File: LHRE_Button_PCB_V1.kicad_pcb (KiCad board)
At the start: 2 copper layers, 146.5 x 78.7 mm, 78 parts, among them IC1 LM5155DSSR, IC2 LM5155DSSR, J1 Conn_01x12_Female, J2 Conn_01x12_Female, J3 Conn_01x02_Female, J4 Conn_01x02_Female, Q1 CSD18537NQ5A, Q2 CSD18537NQ5A, SW1 Dashboard_Button, SW2 Dashboard_Button, SW3 Dashboard_Button, SW4 Dashboard_Button, SW5 Dashboard_Button, SW6 Dashboard_Button

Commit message: REV2
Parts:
- removed C13, C14, C16: 10u, Capacitor_SMD:C_0603_1608Metric
- removed C15, C22: 100p, Capacitor_SMD:C_0603_1608Metric
- removed C17: 270p, Capacitor_SMD:C_0603_1608Metric
- removed C18: 100n, Capacitor_SMD:C_0603_1608Metric
- removed C19: 220n, Capacitor_SMD:C_0603_1608Metric
- removed C20: 6.8n, Capacitor_SMD:C_0603_1608Metric
- removed C21: 1u, Capacitor_SMD:C_0603_1608Metric
- removed C23: 9.4u, Capacitor_SMD:C_0603_1608Metric
- removed C24: 66u, Capacitor_SMD:C_0603_1608Metric
- removed the D1 at (88.5, 62.5)
- removed D2: LED, Connector_Wire:SolderWire-0.75sqmm_1x02_P4.8mm_D1.25mm_OD2.3mm
- removed D4: STPS20M100SG-TR, Global Libraries_2:STPS20M100SG-TR
- removed IC2: LM5155DSSR, Global Libraries_2:SON50P200X300X80-13N-D
- removed L2: 7448700015, Inductor Thing:WE-DD_12XX_CROSSED12
- removed Q2: CSD18537NQ5A, Global Libraries_2:CSD19531Q5AT
- removed the R21 at (182.1, 87.6)
- removed the R22 at (186.2, 89.6)
- removed the R23 at (182.1, 85.8)
- removed the R24 at (182.1, 84.0)
- removed the R25 at (189.3, 45.5)
- removed the R26 at (185.7, 45.5)
- removed the R7 at (204.6, 80.7)
- removed the SW4 at (199.9, 44.8)
- added J5: Conn_01x08, Connector_Molex:Molex_Micro-Fit_3.0_43650-0800_1x08_P3.00mm_Horizontal, F.Cu at (172.0, 80.0)
- added J6: Conn_01x12, Connector_Molex:Molex_Micro-Fit_3.0_43045-1212_2x06_P3.00mm_Vertical, F.Cu at (222.0, 51.0)
- added J7: Conn_01x02, Connector_Molex:Molex_Micro-Fit_3.0_43650-0215_1x02_P3.00mm_Vertical, F.Cu at (109.0, 76.0)
- added R1: 10k, Resistor_SMD:R_0603_1608Metric, F.Cu at (142.5, 40.0)
- added R10: 470, Resistor_SMD:R_0603_1608Metric, F.Cu at (125.5, 76.7)
- added R11: 470, Resistor_SMD:R_0603_1608Metric, F.Cu at (127.9, 95.9)
- added R12: 10k, Resistor_SMD:R_0603_1608Metric, F.Cu at (178.8, 56.5)
- added R13: 10k, Resistor_SMD:R_0603_1608Metric, F.Cu at (176.3, 56.5)
- added R14: 10k, Resistor_SMD:R_0603_1608Metric, F.Cu at (180.8, 83.5)
- added R15: 10k, Resistor_SMD:R_0603_1608Metric, F.Cu at (178.3, 83.5)
- added R16: 10k, Resistor_SMD:R_0603_1608Metric, F.Cu at (178.9, 102.6)
- added R17: 10k, Resistor_SMD:R_0603_1608Metric, F.Cu at (176.3, 102.6)
- added R9: 470, Resistor_SMD:R_0603_1608Metric, F.Cu at (127.8, 50.2)
- added SW1: SW_DIP_x06, Through_DIP_6:18253604, F.Cu at (145.0, 44.4)
- added SW10: Dashboard_Button, Dashboard_LED:Dashboard_Btn, F.Cu at (199.9, 44.8)
- added SW11: Dashboard_Button, Dashboard_LED:Dashboard_Btn, F.Cu at (199.9, 65.1)
- added SW12: Dashboard_Button, Dashboard_LED:Dashboard_Btn, F.Cu at (199.9, 85.4)
- added SW7: SW_DIP_x06, Through_DIP_6:18253604, F.Cu at (176.3, 52.0)
- added SW8: SW_DIP_x06, Through_DIP_6:18253604, F.Cu at (178.3, 79.1)
- added SW9: SW_DIP_x06, Through_DIP_6:18253604, F.Cu at (176.3, 98.1)
- C1, C10, C11, C12, C2, C3, C4, C5, C6, C7, C8, C9, IC1, L1, Q1: moved to B.Cu
- D1: renamed from D3; moved to B.Cu
- J1, J2: value Conn_01x12_Female -> Conn_01x02; footprint Connector_Molex:Molex_Micro-Fit_3.0_43650-1210_1x12-1MP_P3.00mm_Horizontal -> Connector_Molex:Molex_Micro-Fit_3.0_43650-0215_1x02_P3.00mm_Vertical
- J3: value Conn_01x02_Female -> Conn_01x02; footprint Connector_Molex:Molex_Micro-Fit_3.0_43650-0210_1x02-1MP_P3.00mm_Horizontal -> Connector_Molex:Molex_Micro-Fit_3.0_43650-0215_1x02_P3.00mm_Vertical
- J4: value Conn_01x02_Female -> Conn_01x08; footprint Connector_Wire:SolderWire-0.75sqmm_1x02_P4.8mm_D1.25mm_OD2.3mm -> Connector_Molex:Molex_Micro-Fit_3.0_43650-0800_1x08_P3.00mm_Horizontal
- R18: value 6k8 -> 470
- R19: value 34k8 -> 470
- R2, R3, R4, R5, R6: value 1K -> 10k
- R20: value 17k8 -> 470
- R21: renamed from R9; moved to B.Cu
- R22: renamed from R10; moved to B.Cu
- R23: renamed from R11; moved to B.Cu
- R24: renamed from R12; moved to B.Cu
- R25: renamed from R13; moved to B.Cu
- R26: renamed from R14; moved to B.Cu
- R27: renamed from R15; moved to B.Cu
- R28: renamed from R16; moved to B.Cu
- R29: renamed from R17; moved to B.Cu
- SW2, SW3: value Dashboard_Button -> SW_DIP_x06; footprint Dashboard_LED:Dashboard_Btn -> Through_DIP_6:18253604
- moved SW5 78.0 mm to (122.0, 65.1)
- moved SW6 78.0 mm to (122.0, 85.4)
- moved R5 76.9 mm to (142.5, 86.0), turned to -90 degrees
- moved R6 64.9 mm to (145.0, 86.0), turned to -90 degrees
- moved J2 46.0 mm to (208.2, 53.2), turned to -90 degrees
- moved R18 43.2 mm to (193.2, 50.8), turned to -90 degrees
- moved J1 42.0 mm to (109.0, 56.0), turned to 90 degrees
- moved J3 41.9 mm to (208.1, 73.6), turned to -90 degrees
- moved SW3 38.8 mm to (145.0, 90.5), turned to -90 degrees
- moved SW2 36.8 mm to (142.8, 71.5), turned to -90 degrees
- moved R4 34.5 mm to (142.9, 67.1), turned to -90 degrees
- moved R2 33.9 mm to (145.0, 40.0), turned to -90 degrees
- moved C2 32.8 mm to (149.6, 85.8)
- moved J4 32.2 mm to (149.2, 59.0), turned to -90 degrees
- moved C4 29.9 mm to (147.8, 85.8)
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- renumbered R1 to R7, SW1 to SW4
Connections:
- J1 pad 1: AMS -> Net-(J1-Pad1)
- J1 pad 2: 12V_L -> GND1
- J2 pad 1: GND -> Net-(J2-Pad1)
- J2 pad 2: Vin_R -> GND
- J3 pad 2: SHTDWN_OUT -> INRTA_IN_R
- J4 pad 1: SHTDWN_IN -> SW1_OUT
- J4 pad 2: SHTDWN_OUT -> AMS
- R18 pad 1: /SEPIC_CAD_R/UVLO -> G41
- R18 pad 2: GND -> Net-(R18-Pad2)
- R19 pad 1: Vin_R -> G51
- R19 pad 2: /SEPIC_CAD_R/UVLO -> Net-(R19-Pad2)
- R2 pad 2: SW1_OUT -> Net-(R2-Pad2)
- R20 pad 1: GND -> G61
- R20 pad 2: /SEPIC_CAD_R/RT -> Net-(R20-Pad2)
- R3 pad 1: GND1 -> 12V_L
- R3 pad 2: SW2_OUT -> Net-(R3-Pad2)
- R4 pad 2: SW3_OUT -> Net-(R4-Pad2)
- R5 pad 1: GND -> 12V_L
- R5 pad 2: SW4_OUT -> Net-(R5-Pad2)
- R6 pad 1: GND -> GND1
- R6 pad 2: SW5_OUT -> Net-(R6-Pad2)
- R7 pad 2: Net-(D1-Pad2) -> Net-(J1-Pad1)
- R8 pad 2: Net-(D2-Pad2) -> Net-(J2-Pad1)
- SW2 pad 1: 12V_L -> Net-(R4-Pad2)
- SW2 pad 2: SW2_OUT -> Net-(R3-Pad2)
- SW2 pad 3: unconnected-(SW2-Pad3) -> SW2_OUT
- SW2 pad 4: MCU_SIG2 -> SW2_OUT
- SW2 pad 5: GND1 -> 12V_L
- SW3 pad 1: 12V_L -> Net-(R6-Pad2)
- SW3 pad 2: SW3_OUT -> Net-(R5-Pad2)
- SW3 pad 3: unconnected-(SW3-Pad3) -> SW3_OUT
- SW3 pad 4: MCU_SIG3 -> SW3_OUT
- SW3 pad 5: GND1 -> 12V_L
- SW4 pad 1: 12V_L -> SW1_IN
- SW4 pad 4: MCU_SIG1 -> P11
- SW4 pad 5: GND1 -> Net-(R9-Pad2)
- SW5 pad 1: 12V_R -> SW2_IN
- SW5 pad 2: SW5_OUT -> SW2_OUT
- SW5 pad 4: MCU_SIG5 -> P21
- SW5 pad 5: GND -> Net-(R10-Pad2)
- SW6 pad 1: 12V_R -> SW3_IN
- SW6 pad 2: SW6_OUT -> SW3_OUT
- SW6 pad 4: MCU_SIG6 -> P31
- SW6 pad 5: GND -> Net-(R11-Pad2)
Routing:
- net 12V_L: track 181.4 -> 92.4 mm, vias 0 -> 1
- net /SEPIC_CAD_R/FB: track 69.1 -> 0.00 mm
- net MCU_SIG3: track 60.9 -> 0.00 mm, vias 2 -> 0
- net SW3_OUT_R: track 0.00 -> 59.5 mm, vias 0 -> 2
- net GND: track 55.8 -> 0.00 mm, vias 18 -> 9
- net SW1_OUT_R: track 0.00 -> 55.3 mm
- net SW2_OUT_R: track 0.00 -> 54.8 mm
- net SHTDWN_OUT_R: track 0.00 -> 51.8 mm
- net AMS_R: track 0.00 -> 50.3 mm
- net MCU_SIG1: track 46.6 -> 0.00 mm
- net MCU_SIG2: track 46.6 -> 0.00 mm
- net INRTA_IN: track 0.00 -> 44.3 mm, vias 0 -> 2
- net 12V_R: track 139.7 -> 96.0 mm
- net SW2_IN: track 0.00 -> 43.2 mm
- net Net-(C11-Pad1): track 16.6 -> 58.7 mm
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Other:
- board size 146.5 x 78.7 mm -> 131.7 x 78.7 mm

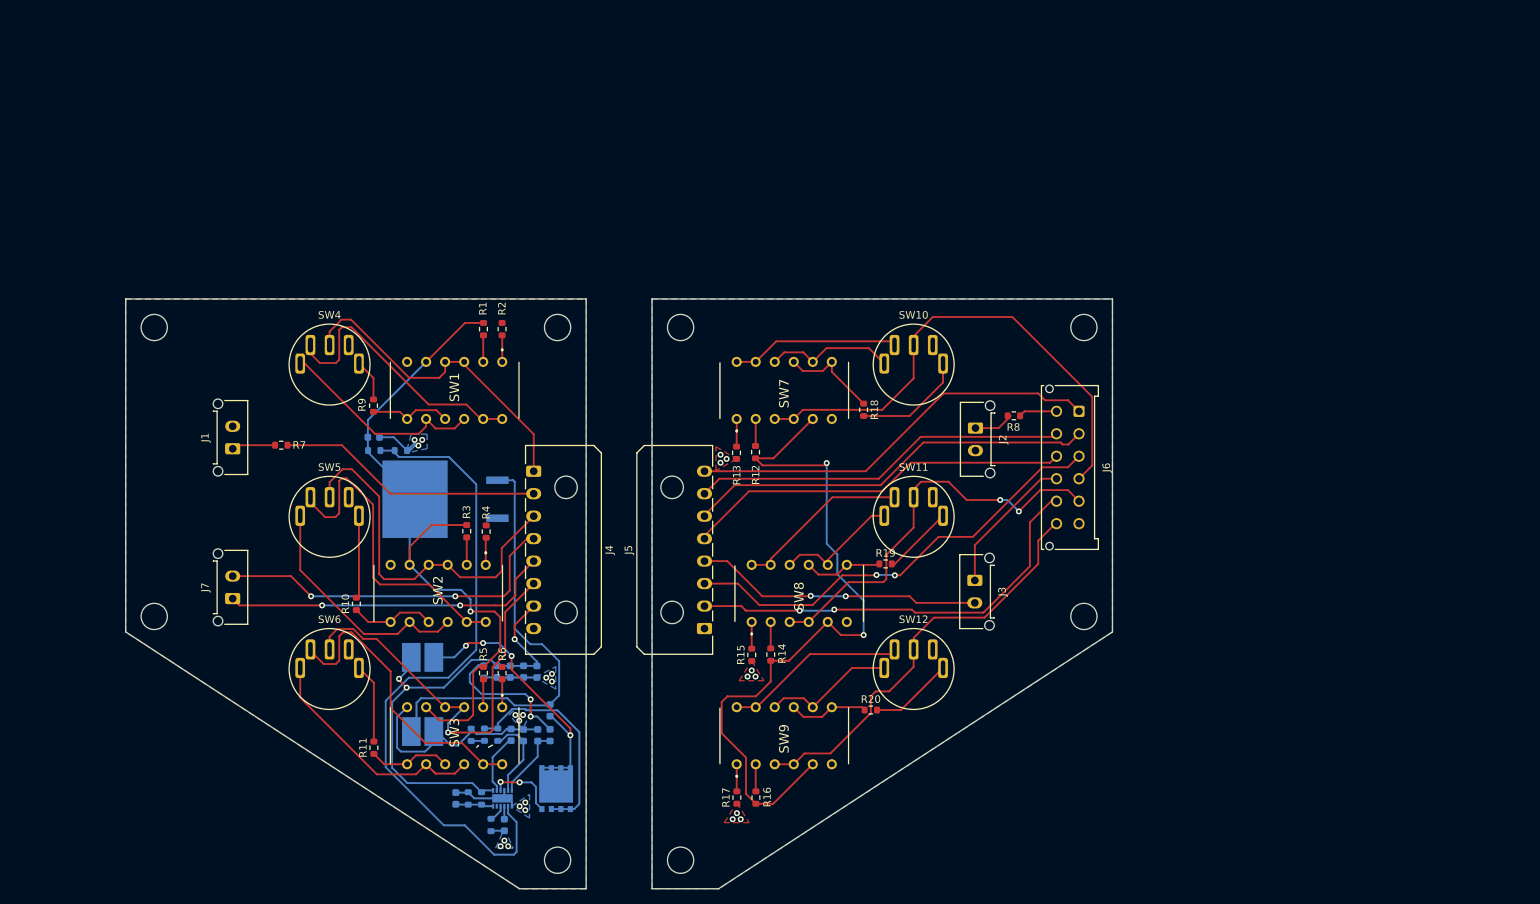
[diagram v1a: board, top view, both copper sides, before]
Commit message: flipped connectors
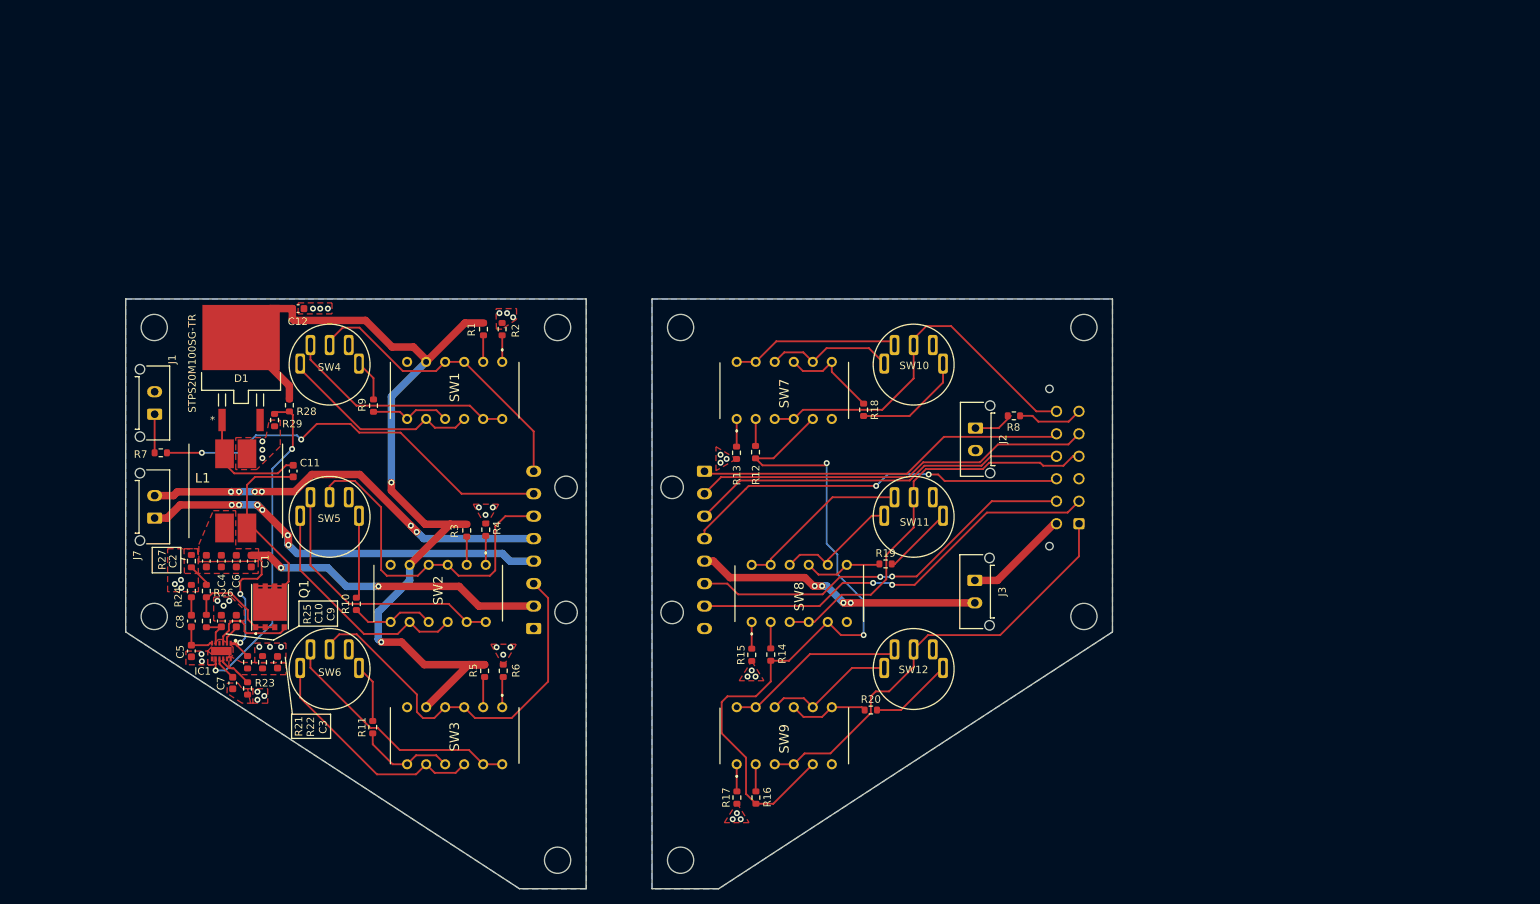
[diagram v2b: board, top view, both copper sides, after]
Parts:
- C1, C10, C11, C12, C2, C3, C4, C5, C6, C7, C8, C9, D1, IC1, L1, Q1, R21, R22, R23, R24, R25, R26, R27, R28, R29: moved to F.Cu
- J4, J5, J6: moved to B.Cu
- moved C8 50.3 mm to (103.5, 79.0)
- moved C5 47.6 mm to (103.5, 83.0), turned to -90 degrees
- moved C11 46.9 mm to (117.1, 59.0)
- moved C2 46.5 mm to (105.5, 71.0)
- moved Q1 45.3 mm to (114.0, 77.4)
- moved R27 44.0 mm to (103.5, 71.0)
- moved C10 43.1 mm to (107.5, 79.0)
- moved C4 43.0 mm to (107.5, 71.0)
- moved IC1 42.4 mm to (107.5, 83.0)
- moved R26 41.8 mm to (105.5, 75.0), turned to 90 degrees
- moved R25 41.8 mm to (105.5, 79.0)
- moved C7 40.9 mm to (109.0, 87.3)
- moved R24 40.5 mm to (103.5, 75.0), turned to 90 degrees
- moved C9 39.7 mm to (109.5, 79.0)
- moved C6 39.4 mm to (109.5, 71.0)
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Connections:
- J4 pad 1: SW1_OUT -> GND1
- J4 pad 2: AMS -> Vin_L
- J4 pad 3: SW2_OUT -> SW3_OUT
- J4 pad 4: SHTDWN_OUT -> INRTA_IN
- J4 pad 5: INRTA_IN -> SHTDWN_OUT
- J4 pad 6: SW3_OUT -> SW2_OUT
- J4 pad 7: Vin_L -> AMS
- J4 pad 8: GND1 -> SW1_OUT
- J5 pad 1: GND -> SW1_OUT_R
- J5 pad 2: Vin_R -> AMS_R
- J5 pad 3: SW3_OUT_R -> SW2_OUT_R
- J5 pad 4: INRTA_IN_R -> SHTDWN_OUT_R
- J5 pad 5: SHTDWN_OUT_R -> INRTA_IN_R
- J5 pad 6: SW2_OUT_R -> SW3_OUT_R
- J5 pad 7: AMS_R -> Vin_R
- J5 pad 8: SW1_OUT_R -> GND
- J6 pad 1: SW1_OUT_R -> SW6_OUT
- J6 pad 10: SHTDWN_IN -> SW2_OUT_R
- J6 pad 11: Vin_R -> SW1_OUT_R
- J6 pad 12: SW6_OUT -> SW4_OUT
- J6 pad 2: SW2_OUT_R -> Vin_R
- J6 pad 3: SW3_OUT_R -> GND
- J6 pad 4: SW4_OUT -> SW5_OUT
- J6 pad 5: SW5_OUT -> AMS_R
- J6 pad 6: GND -> IMD
- J6 pad 7: IMD -> SHTDWN_IN
- J6 pad 8: AMS_R -> SW3_OUT_R
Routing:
- net GND1: track 56.7 -> 0.07 mm, vias 15 -> 29
- net /SEPIC_CAD/FB: track 89.7 -> 43.5 mm, vias 0 -> 2
- net Net-(C11-Pad1): track 58.7 -> 16.1 mm
- net 12V_L: track 92.4 -> 127.0 mm, vias 1 -> 2
- net AMS: track 35.6 -> 54.9 mm, vias 0 -> 2
- net SW4_OUT: track 67.4 -> 50.6 mm
- net Net-(C8-Pad2): track 18.1 -> 2.40 mm, vias 2 -> 0
- net Net-(Q1-Pad1): track 29.0 -> 14.3 mm
- net INRTA_IN: track 44.3 -> 58.4 mm, vias 2 -> 6
- net SHTDWN_OUT: track 47.2 -> 58.5 mm, vias 2 -> 6
- net Net-(C11-Pad2): track 37.8 -> 27.0 mm, vias 4 -> 0
- net SW2_IN: track 43.2 -> 35.6 mm
- net Net-(C10-Pad2): track 11.6 -> 4.51 mm
- net SW3_IN: track 40.3 -> 33.4 mm
- net SW3_OUT_R: track 59.5 -> 52.7 mm
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- added copper zone on F.Cu, net /SEPIC_CAD/UVLO
- added copper zone on F.Cu, net Vin_L

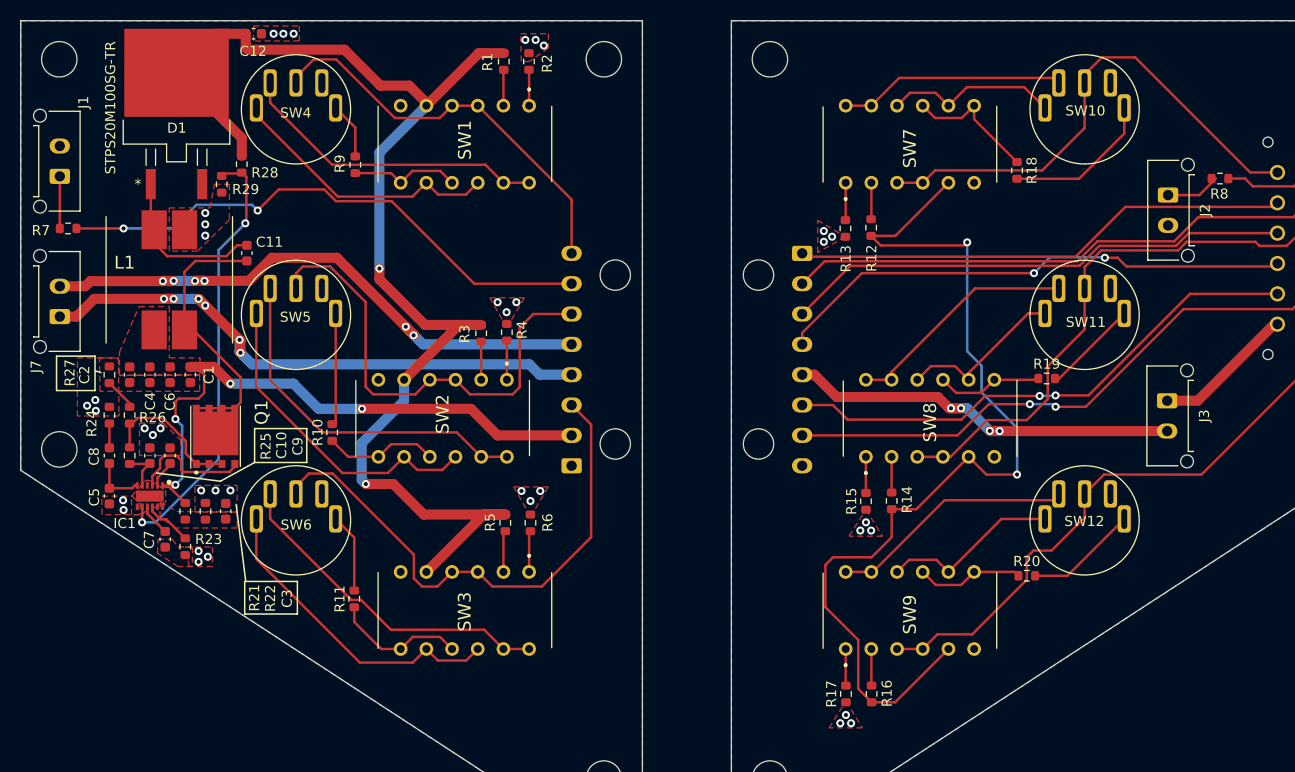
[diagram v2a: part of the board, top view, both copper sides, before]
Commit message: changeed caps
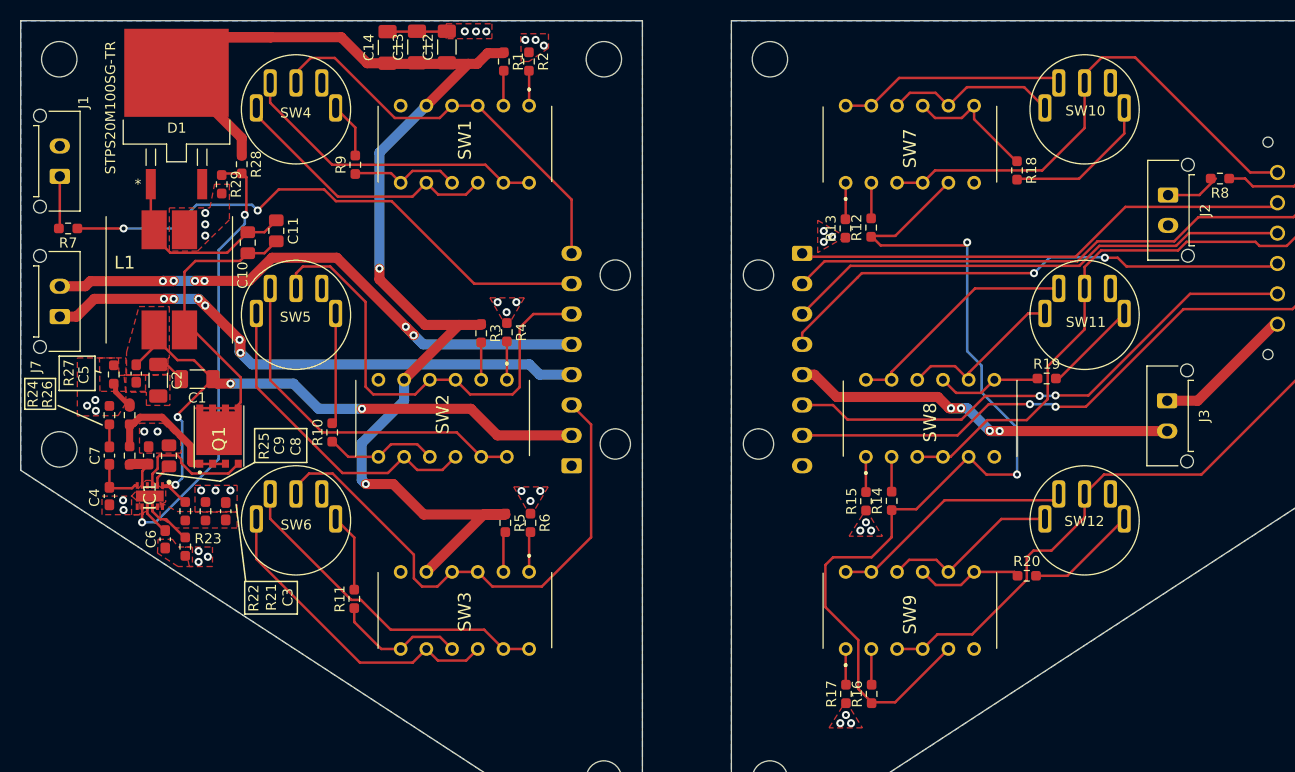
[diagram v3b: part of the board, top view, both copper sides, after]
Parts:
- removed the C4 at (107.5, 71.0)
- added C11: 4.7u, Capacitor_SMD:C_0805_2012Metric_Pad1.18x1.45mm_HandSolder, F.Cu at (120.0, 56.8)
- added C12: 22u, Capacitor_SMD:C_1206_3216Metric_Pad1.33x1.80mm_HandSolder, F.Cu at (136.9, 38.6)
- added C13: 22u, Capacitor_SMD:C_1206_3216Metric_Pad1.33x1.80mm_HandSolder, F.Cu at (133.9, 38.6)
- C1, C2: value 10u -> 22u; footprint Capacitor_SMD:C_0603_1608Metric -> Capacitor_SMD:C_1206_3216Metric_Pad1.33x1.80mm_HandSolder
- C10: renamed from C11; value 9.4u -> 4.7u; footprint Capacitor_SMD:C_0603_1608Metric -> Capacitor_SMD:C_0805_2012Metric_Pad1.18x1.45mm_HandSolder
- C14: renamed from C12; value 66u -> 22u; footprint Capacitor_SMD:C_0603_1608Metric -> Capacitor_SMD:C_1206_3216Metric_Pad1.33x1.80mm_HandSolder
- C3: footprint Capacitor_SMD:C_0603_1608Metric -> Capacitor_SMD:C_0603_1608Metric_Pad1.08x0.95mm_HandSolder
- C4: renamed from C5; footprint Capacitor_SMD:C_0603_1608Metric -> Capacitor_SMD:C_0603_1608Metric_Pad1.08x0.95mm_HandSolder
- C5: renamed from C6; footprint Capacitor_SMD:C_0603_1608Metric -> Capacitor_SMD:C_0603_1608Metric_Pad1.08x0.95mm_HandSolder
- C6: renamed from C7; footprint Capacitor_SMD:C_0603_1608Metric -> Capacitor_SMD:C_0603_1608Metric_Pad1.08x0.95mm_HandSolder
- C7: renamed from C8; footprint Capacitor_SMD:C_0603_1608Metric -> Capacitor_SMD:C_0603_1608Metric_Pad1.08x0.95mm_HandSolder
- C8: renamed from C9; footprint Capacitor_SMD:C_0603_1608Metric -> Capacitor_SMD:C_0805_2012Metric_Pad1.18x1.45mm_HandSolder
- C9: renamed from C10; footprint Capacitor_SMD:C_0603_1608Metric -> Capacitor_SMD:C_0603_1608Metric_Pad1.08x0.95mm_HandSolder
- R1, R10, R11, R12, R13, R14, R15, R16, R17, R18, R19, R2, R20, R21, R22, R23, R24, R25, R26, R27, R28, R29, R3, R4, R5, R6, R7, R8, R9: footprint Resistor_SMD:R_0603_1608Metric -> Resistor_SMD:R_0603_1608Metric_Pad0.98x0.95mm_HandSolder
- moved C14 13.3 mm to (131.0, 38.6), turned to 90 degrees
- moved C5 3.35 mm to (106.2, 70.9)
- moved C2 2.88 mm to (108.3, 71.5)
- moved C10 1.03 mm to (117.2, 57.9)
- moved C1 0.81 mm to (112.2, 71.4), turned to 180 degrees
- moved R27 0.43 mm to (103.9, 71.0)
- moved Q1 0.35 mm to (114.3, 77.3)
- moved C9 0.12 mm to (107.4, 79.0)
- moved C8 0.11 mm to (109.4, 79.0)
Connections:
- C1 pad 2: GND1 -> Net-(C1-Pad2)
- C2 pad 1: Vin_L -> Net-(C1-Pad2)
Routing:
- net 12V_L: track 127.0 -> 139.0 mm
- net Vin_L: track 61.8 -> 68.3 mm
- net GND1: track 0.07 -> 5.95 mm, vias 29 -> 28
- net Net-(C10-Pad2): track 27.0 -> 30.7 mm
- net Net-(C10-Pad1): track 16.1 -> 19.4 mm
- net Net-(C1-Pad2): track 0.00 -> 2.89 mm
- net SW1_OUT: track 40.6 -> 41.6 mm
- net Net-(Q1-Pad1): track 14.3 -> 14.9 mm
